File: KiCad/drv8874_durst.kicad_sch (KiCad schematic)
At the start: 25 parts, among them J1 TM1638 Led&Key Module Connect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, J2 Barrel_Jack, J3 Grove LCD 4 Pin I2C, M1_LensMotor1 Motor_DC_ALT, M2_HeadMotor1 Motor_DC_ALT, SW1 SW_LensUpperLimit_NC, SW2 SW_LensLowerLimit_NC, SW3 SW_HeadUpperLimit_NC, SW4 SW_HeadLowerLimit_NC, U1 SSR AD Relay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

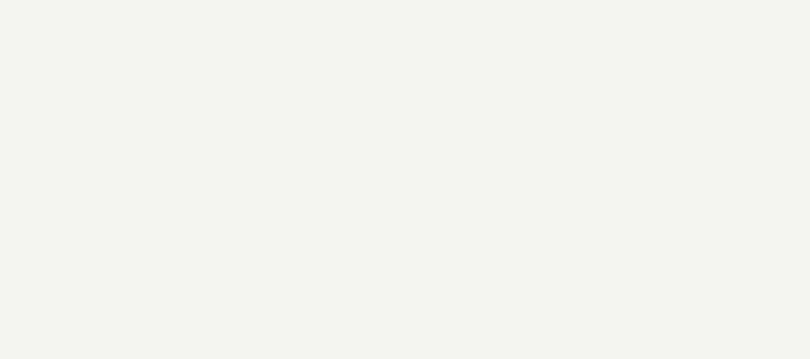
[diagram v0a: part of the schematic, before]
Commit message: kicad : add relay
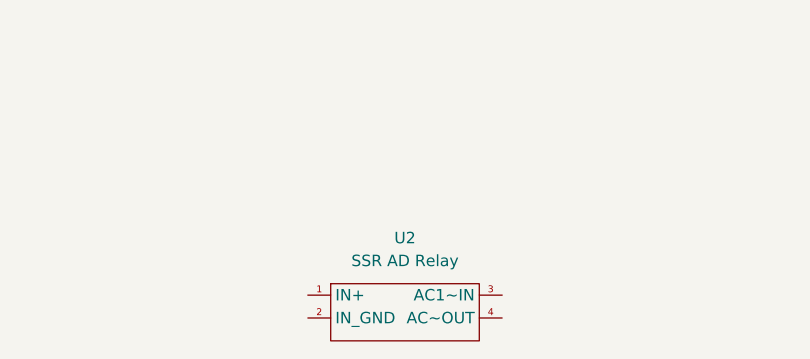
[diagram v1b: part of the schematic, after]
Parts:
- added U2: SSR AD Relay, symbol petro:SSR_Relay
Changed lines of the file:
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@@
+	)
+	(symbol
+		(lib_id "petro:SSR_Relay")
+		(at 77.47 161.29 0)
+		(unit 1)
+		(exclude_from_sim no)
+		(in_bom yes)
+		(on_board yes)
+		(dnp no)
+		(fields_autoplaced yes)
+		(property "Reference" "U2"
+			(at 79.375 157.48 0)
+			(effects
+				(font
+					(size 1.27 1.27)
+				)
+			)
+		)
+		(property "Value" "SSR AD Relay"
+			(at 79.375 160.02 0)
+			(effects
+				(font
+					(size 1.27 1.27)
+				)
+			)
+		)
+		(property "Footprint" ""
+			(at 77.47 161.29 0)
+			(effects
+				(font
+					(size 1.27 1.27)
+				)
+				(hide yes)
+			)
+		)
+		(property "Datasheet" ""
+			(at 77.47 161.29 0)
+			(effects
+				(font
+					(size 1.27 1.27)
+				)
+				(hide yes)
+			)
+		)
+		(property "Description" ""
+			(at 77.47 161.29 0)
+			(effects
+				(font
+					(size 1.27 1.27)
+				)
+				(hide yes)
+			)
+		)
+		(pin "4"
+		)
+		(pin "2"
+		)
+		(pin "1"
+		)
+		(pin "3"
+		)
+		(instances
+			(project ""
+				(path "/824d854a-3366-45dc-a9ec-858fab4cff49"
+					(reference "U2")
+					(unit 1)
+				)
+			)
+		)
 	)
 	(symbol
